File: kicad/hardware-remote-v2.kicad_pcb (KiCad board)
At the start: 2 copper layers, 130 x 70 mm, 29 parts, among them J1 Flash, J2 TFT, J3 5VIN, J4 3.3VIN, J5 Conn_02x08_Odd_Even, Q1 2N7002, SW1 ANALOG_LEFT, SW2 ANALOG_RIGHT, U1 ESP32-WROOM-32E-8MB, U2 AMS1117-3.3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

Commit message: Production files
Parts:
- added C8: 100n, Capacitor_SMD:C_0603_1608Metric, F.Cu at (7.00, 28.2)
- added C9: 100n, Capacitor_SMD:C_0603_1608Metric, F.Cu at (15.8, 20.2)
- added Q2: SS8050_C2150, SS8050:SOT-23-3_L2.9-W1.3-P1.90-LS2.4-BR, F.Cu at (32.4, -19.8)
- added Q3: SS8050_C2150, SS8050:SOT-23-3_L2.9-W1.3-P1.90-LS2.4-BR, F.Cu at (31.6, -15.1)
- added R7: 12k, Resistor_SMD:R_0603_1608Metric, F.Cu at (29.2, -17.7)
- added R8: 12k, Resistor_SMD:R_0603_1608Metric, F.Cu at (35.0, -16.4)
- R1: value 47k -> 10k
- R2: value 15k -> 10k
- moved J4 2.50 mm to (21.6, 25.9), turned to 180 degrees
- moved C4 0.30 mm to (24.7, 24.6), turned to -90 degrees
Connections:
- U3 pad 10: IO0 -> DTR
- U3 pad 11: EN -> RTS
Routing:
- net RTS: track 0.00 -> 14.4 mm
- net DTR: track 0.00 -> 8.70 mm
- net Net-(Q3-Pad1): track 0.00 -> 5.15 mm
- net EN: track 59.3 -> 64.2 mm
- net IO0: track 72.4 -> 76.6 mm, vias 4 -> 3
- net +3V3: track 57.0 -> 60.8 mm
- net Net-(Q2-Pad1): track 0.00 -> 2.35 mm
- net +5V: track 174.0 -> 176.3 mm
- net USB_DN: track 63.9 -> 62.6 mm
- net GND: track 80.8 -> 81.2 mm, vias 31 -> 29
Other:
- outline, holes or cut-outs redrawn
- board text added: "3V3"
- board text added: "5V"

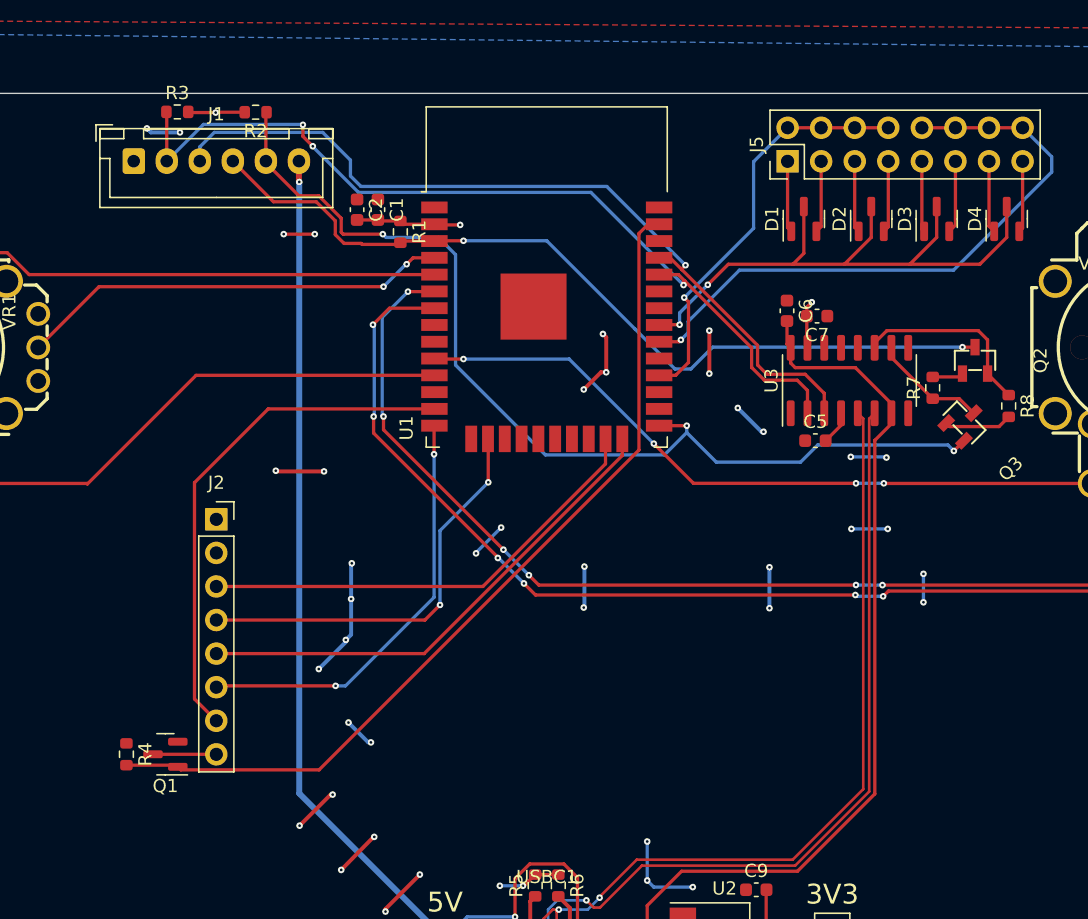
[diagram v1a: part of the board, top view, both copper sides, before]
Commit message: Updated / fixed pcb
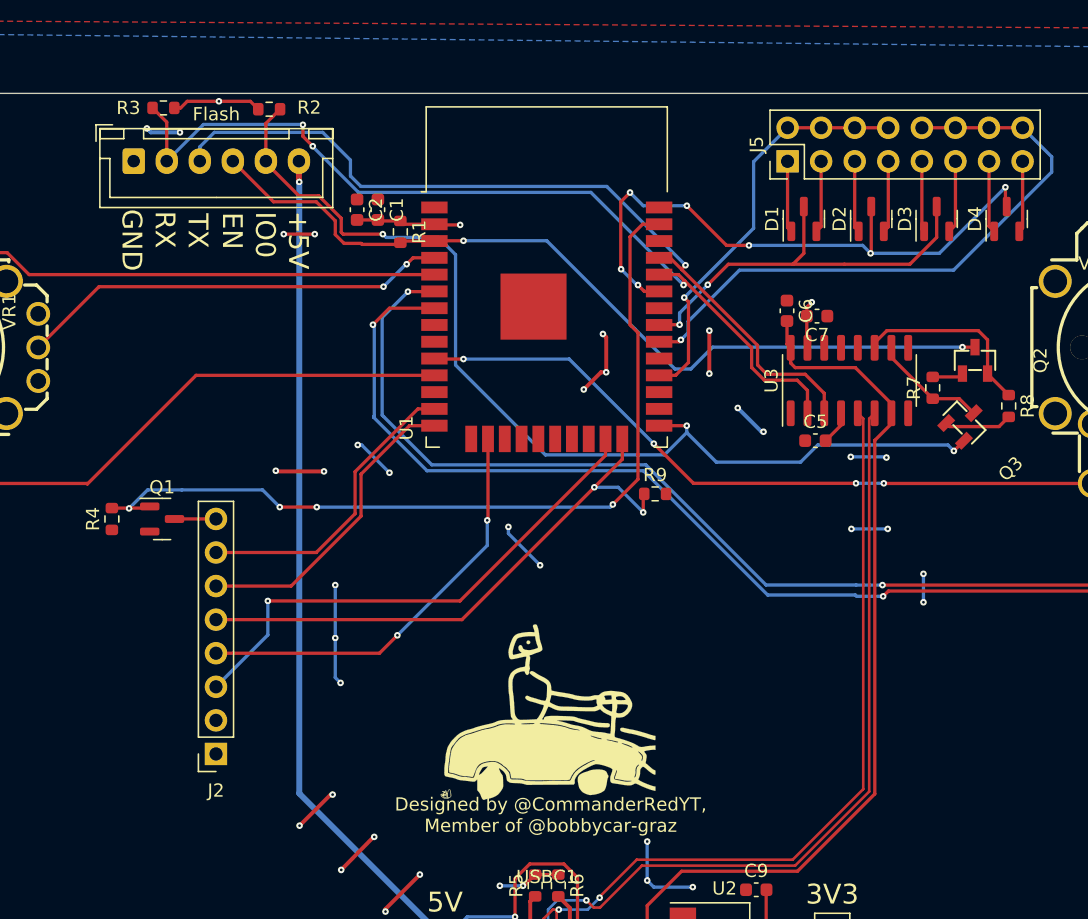
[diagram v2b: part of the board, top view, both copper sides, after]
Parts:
- added G***: LOGO, Logo:lenas_bobbycar_logo, F.Cu at (0.10, 8.30)
- added R9: 10k, Resistor_SMD:R_0603_1608Metric, F.Cu at (8.20, -9.70)
- moved R4 17.8 mm to (-32.9, -7.80), turned to 90 degrees
- moved Q1 17.8 mm to (-29.1, -7.80), turned to 0 degrees
- moved J2 17.8 mm to (-25.0, 9.97), turned to 180 degrees
- moved R3 1.09 mm to (-29.0, -38.9)
- moved R2 1.05 mm to (-21.0, -38.8)
- renumbered J1 to Flash
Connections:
- D1 pad 3: BUTTON_OUT -> BUTTON_OUT1
- D2 pad 3: BUTTON_OUT -> BUTTON_OUT2
- D3 pad 3: BUTTON_OUT -> BUTTON_OUT1
- D4 pad 3: BUTTON_OUT -> BUTTON_OUT2
- U1 pad 31: BUTTON_OUT -> BUTTON_OUT1
- U1 pad 33: unconnected-(U1-Pad33) -> BUTTON_OUT2
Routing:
- net BUTTON_OUT2: track 0.00 -> 47.1 mm, vias 0 -> 7
- net BUTTON_OUT: track 47.0 -> 0.00 mm, vias 2 -> 0
- net BUTTON_OUT1: track 0.00 -> 31.3 mm, vias 0 -> 2
- net CS: track 39.2 -> 22.9 mm
- net TFT_DC: track 32.3 -> 23.4 mm, vias 2 -> 0
- net GND: track 81.2 -> 75.6 mm, vias 29 -> 24
- net TFT_RESET: track 38.2 -> 43.2 mm, vias 0 -> 2
- net TFT_SCLK: track 35.2 -> 39.5 mm, vias 0 -> 1
- net TFT_LED: track 67.1 -> 64.6 mm, vias 0 -> 4
- net +3V3: track 60.8 -> 63.3 mm
- net Net-(J2-Pad8): track 4.79 -> 3.14 mm
- net ESP_RX: track 67.3 -> 68.1 mm
- net ANALOG_RIGHT_Y: track 116.3 -> 115.5 mm, vias 6 -> 2
- net IO0: track 76.6 -> 77.3 mm
- net ANALOG_RIGHT_X: track 97.9 -> 97.3 mm, vias 6 -> 2
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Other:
- board text added: "+5V"
- board text added: "Designed by @CommanderRedYT, Member of @bobbycar-graz"
- board text added: "EN"
- board text added: "GND"
- board text added: "IO0"
- board text added: "RX"
- board text added: "TX"
